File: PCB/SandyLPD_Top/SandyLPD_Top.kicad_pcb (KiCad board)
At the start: 2 copper layers, 30.3 x 23 mm, 18 parts

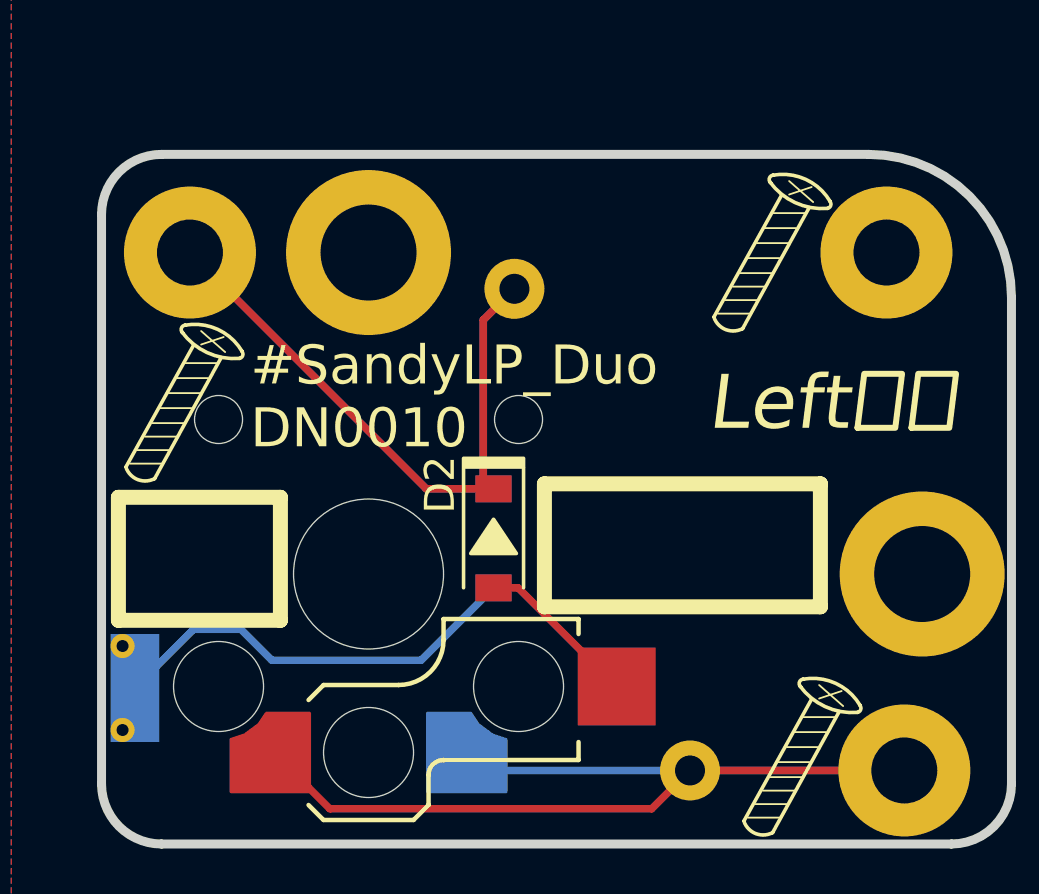
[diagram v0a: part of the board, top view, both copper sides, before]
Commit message: 電源LED位置調整。ボトムA,Bのリセット穴サイズ変更。Fusion用STEP出力。
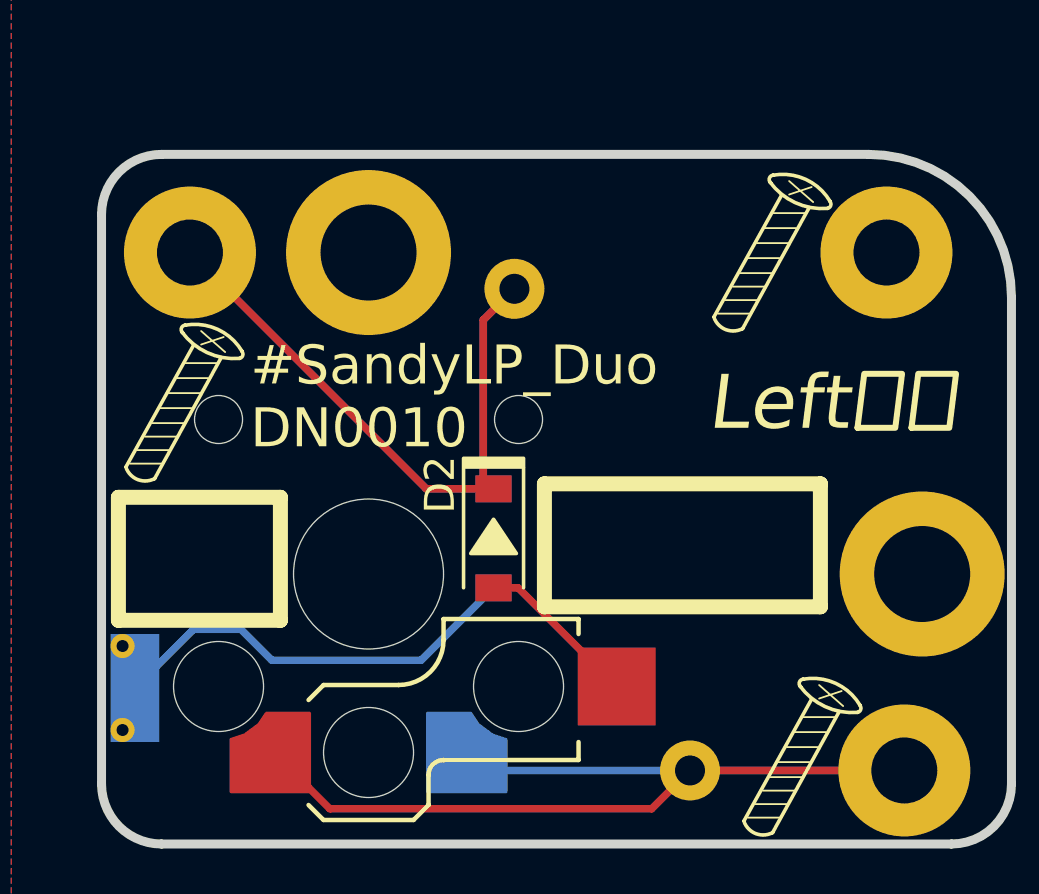
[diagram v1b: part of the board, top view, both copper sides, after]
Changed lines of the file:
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@@
 		(allow_soldermask_bridges_in_footprints no)
 		(aux_axis_origin 19.86781 34.147155)
-		(grid_origin 19.86781 34.147155)
+		(grid_origin 24.63031 36.528405)
 		(pcbplotparams
 			(layerselection 0x00310fc_ffffffff)
@@
 		(fp_arc
 			(start 2.475824 -5.107131)
-			(mid 1.4 -5.3)
+			(mid 1.399999 -5.299999)
 			(end 0.555319 -5.993622)
 			(stroke
@@
 		(at 122.625342 43.973449)
 		(property "Reference" "REF**"
-			(at 0 0.5 360)
+			(at 0 0.5 0)
 			(layer "Cmts.User")
 			(effects
@@
 		)
 		(property "Value" "ICON_Screw_Long_Medium"
-			(at 0 -0.5 360)
+			(at 0 -0.5 0)
 			(layer "F.Fab")
 			(effects
@@
 		)
 		(property "Footprint" "locallib:ICON_Screw_Long_Medium"
-			(at 0 0 360)
+			(at 0 0 0)
 			(layer "F.Fab")
 			(hide yes)
@@
 		)
 		(property "Datasheet" ""
-			(at 0 0 360)
+			(at 0 0 0)
 			(layer "F.Fab")
 			(hide yes)
@@
 		)
 		(property "Description" ""
-			(at 0 0 360)
+			(at 0 0 0)
 			(layer "F.Fab")
 			(hide yes)
@@
 		(fp_arc
 			(start 0.582958 -5.961016)
-			(mid 0.542326 -6.113994)
+			(mid 0.542323 -6.113993)
 			(end 0.665318 -6.21362)
 			(stroke
@@
 		(fp_arc
 			(start 2.475824 -5.107131)
-			(mid 1.399999 -5.299999)
+			(mid 1.4 -5.3)
 			(end 0.555319 -5.993622)
 			(stroke
@@
 		(fp_arc
 			(start 2.475824 -5.107131)
-			(mid 1.4 -5.3)
+			(mid 1.399999 -5.299999)
 			(end 0.555319 -5.993622)
 			(stroke
@@
 		(fp_arc
 			(start 2.475824 5.107132)
-			(mid 2.585568 5.201267)
+			(mid 2.585576 5.201276)
 			(end 2.557784 5.343159)
 			(stroke
@@
 		(fp_arc
 			(start 2.475824 5.107132)
-			(mid 2.585568 5.201267)
+			(mid 2.585576 5.201276)
 			(end 2.557784 5.343159)
 			(stroke
@@
 		(fp_arc
 			(start 0.555319 5.993622)
-			(mid 1.4 5.300002)
+			(mid 1.4 5.300001)
 			(end 2.475824 5.107131)
 			(stroke
@@
 		(tags "test point THT pad")
 		(property "Reference" "T_R0"
-			(at 0 2.070305 360)
+			(at 0 2.070305 0)
 			(layer "B.SilkS")
 			(effects
@@
 		)
 		(property "Value" "Conn_01x01"
-			(at 0 -2.05 360)
+			(at 0 -2.05 0)
 			(layer "B.Fab")
 			(effects
@@
 		)
 		(fp_text user "${REFERENCE}"
-			(at 0 2 360)
+			(at 0 2 0)
 			(layer "B.Fab")
 			(effects
@@
 		(fp_arc
 			(start 2.475824 5.107132)
-			(mid 2.585568 5.201267)
+			(mid 2.585576 5.201276)
 			(end 2.557784 5.343159)
 			(stroke

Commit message: ネジ穴にスルーホールタップのアイコンを追加
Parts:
- added REF**: ICON_Through-hole_Tap, locallib:ICON_Through-hole_Tap, B.Cu at (129.4, 39.8)
- added REF**: ICON_Through-hole_Tap, locallib:ICON_Through-hole_Tap, F.Cu at (129.4, 39.8)
- added REF**: ICON_Through-hole_Tap, locallib:ICON_Through-hole_Tap, F.Cu at (142.7, 45.4)
- added REF**: ICON_Through-hole_Tap, locallib:ICON_Through-hole_Tap, B.Cu at (142.4, 45.9)
- moved REF** 0.54 mm to (143.7, 39.1)
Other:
- board text added: "Left 左 Back Side"
- board text added: "Right 右 Back Side"
- board text removed: "Left 左"
- board text removed: "Right 右"

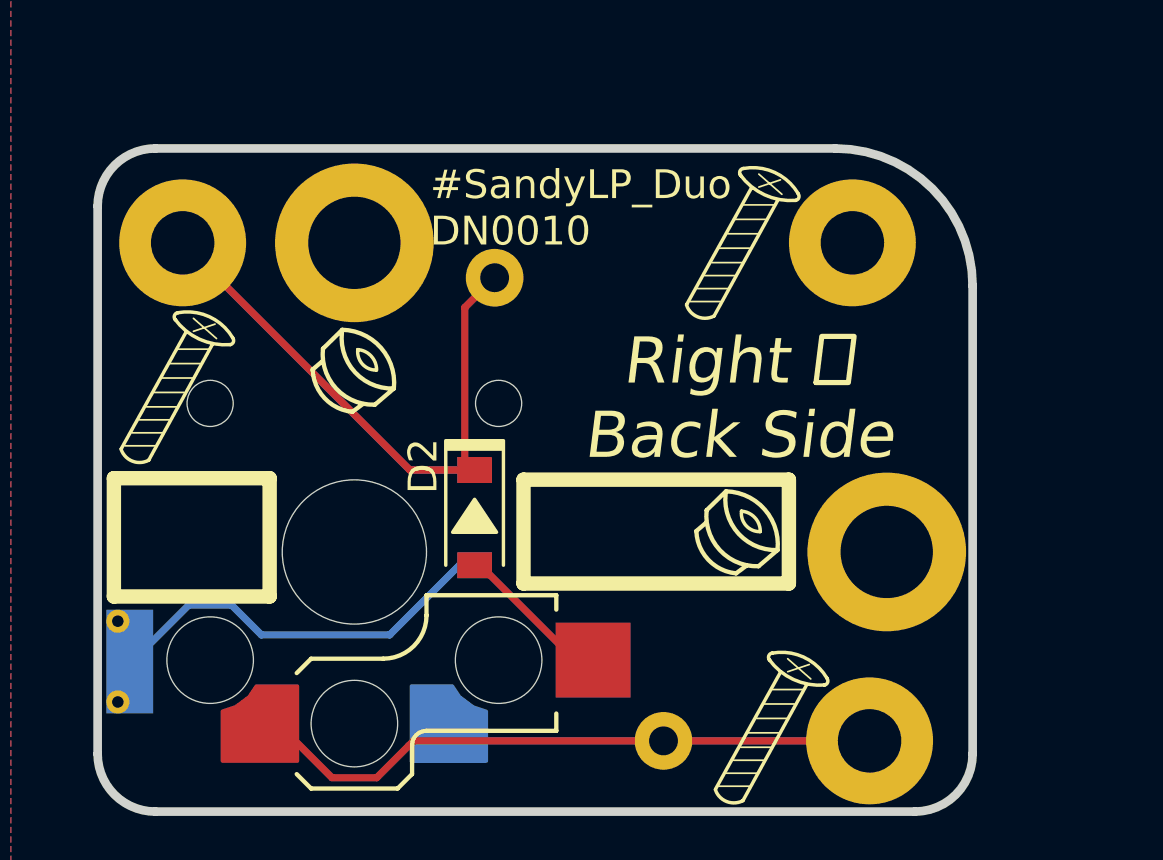
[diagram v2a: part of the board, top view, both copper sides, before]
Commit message: 間違い防止のシルク #30
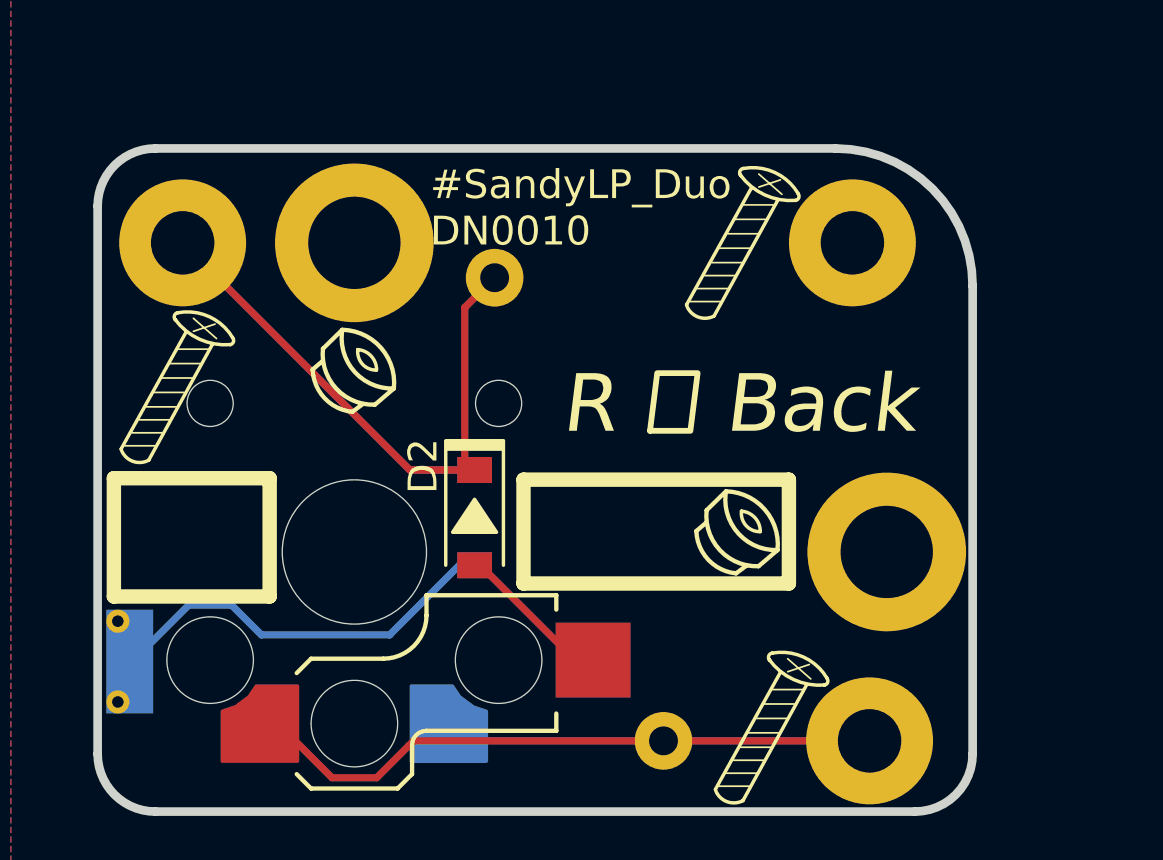
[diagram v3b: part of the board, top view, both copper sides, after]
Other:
- board text added: "L 左 Back"
- board text added: "R 右 Back"
- board text removed: "Left 左 Back Side"
- board text removed: "Right 右 Back Side"
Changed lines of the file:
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@@
 		(fp_arc
 			(start 2.475824 -5.107131)
-			(mid 1.399999 -5.299999)
+			(mid 1.4 -5.3)
 			(end 0.555319 -5.993622)
 			(stroke
@@
 		(fp_arc
 			(start 0.729448 -0.077979)
-			(mid 0.250509 -0.290344)
+			(mid 0.25051 -0.290344)
 			(end 0.092873 -0.789976)
 			(stroke
@@
 		(fp_arc
 			(start 2.475824 -5.107131)
-			(mid 1.4 -5.3)
+			(mid 1.399999 -5.299999)
 			(end 0.555319 -5.993622)
 			(stroke
@@
 		(fp_arc
 			(start 2.475824 -5.107131)
-			(mid 1.399999 -5.299999)
+			(mid 1.4 -5.3)
 			(end 0.555319 -5.993622)
 			(stroke
@@
 		(fp_arc
 			(start 0.729448 -0.077979)
-			(mid 0.250509 -0.290344)
+			(mid 0.25051 -0.290344)
 			(end 0.092873 -0.789976)
 			(stroke
@@
 			(layer "F.SilkS")
 		)
-		(group ""
-			(members "10583bed-aab3-457f-b2ae-f3b5453b8340" "38793d8d-a27c-4080-ae1c-5bc01cf71245"
-				"3ed98f41-62c1-480d-b26d-36dc4ac3c762" "4bf3dc3f-affc-4877-b134-b3363bf5cef2"
-				"53d0ed37-4d95-44d2-b473-0a9a16a8503c" "a00f956a-55b7-46e8-802e-5baff904af2b"
-				"b080e6b3-1454-4fc5-b8b4-c70b5498519d" "d03374e9-98f6-454e-8289-46865e659acf"
-				"f62ba8d0-430f-4730-8b76-93be139405e9" "f8a60fd9-4eb6-4c55-8373-fa38d0a8137c"
-			)
-		)
 	)
 	(footprint "locallib:ICON_Through-hole_Tap"
@@
 			(layer "B.SilkS")
 		)
-		(group ""
-			(members "10583bed-aab3-457f-b2ae-f3b5453b8340" "38793d8d-a27c-4080-ae1c-5bc01cf71245"
-				"3ed98f41-62c1-480d-b26d-36dc4ac3c762" "4bf3dc3f-affc-4877-b134-b3363bf5cef2"
-				"53d0ed37-4d95-44d2-b473-0a9a16a8503c" "a00f956a-55b7-46e8-802e-5baff904af2b"
-				"b080e6b3-1454-4fc5-b8b4-c70b5498519d" "d03374e9-98f6-454e-8289-46865e659acf"
-				"f62ba8d0-430f-4730-8b76-93be139405e9" "f8a60fd9-4eb6-4c55-8373-fa38d0a8137c"
-			)
-		)
 	)
 	(footprint "locallib:Kailh_socket_ChocV2_for_Reverse"
@@
 			(layer "B.SilkS")
 		)
-		(group ""
-			(members "10583bed-aab3-457f-b2ae-f3b5453b8340" "38793d8d-a27c-4080-ae1c-5bc01cf71245"
-				"3ed98f41-62c1-480d-b26d-36dc4ac3c762" "4bf3dc3f-affc-4877-b134-b3363bf5cef2"
-				"53d0ed37-4d95-44d2-b473-0a9a16a8503c" "a00f956a-55b7-46e8-802e-5baff904af2b"
-				"b080e6b3-1454-4fc5-b8b4-c70b5498519d" "d03374e9-98f6-454e-8289-46865e659acf"
-				"f62ba8d0-430f-4730-8b76-93be139405e9" "f8a60fd9-4eb6-4c55-8373-fa38d0a8137c"
-			)
-		)
 	)
 	(gr_rect
@@
 		(layer "F.SilkS")
 	)
-	(gr_text "Left　左\nBack Side"
-		(at 142.93031 40.828405 0)
+	(gr_text "L 左 Back"
+		(at 143.03031 40.928405 0)
 		(layer "B.SilkS" knockout)
 		(effects
 			(font
-				(size 1.6 1.6)
-				(thickness 0.18)
+				(size 2 2)
+				(thickness 0.2)
 				(italic yes)
 			)
@@
 		)
 	)
-	(gr_text "Right 右\nBack Side"
-		(at 142.73031 40.728405 0)
+	(gr_text "R 右 Back"
+		(at 142.73031 40.928405 0)
 		(layer "F.SilkS" knockout)
 		(effects
 			(font
-				(size 1.6 1.6)
-				(thickness 0.18)
+				(size 2 2)
+				(thickness 0.2)
 				(italic yes)
 			)

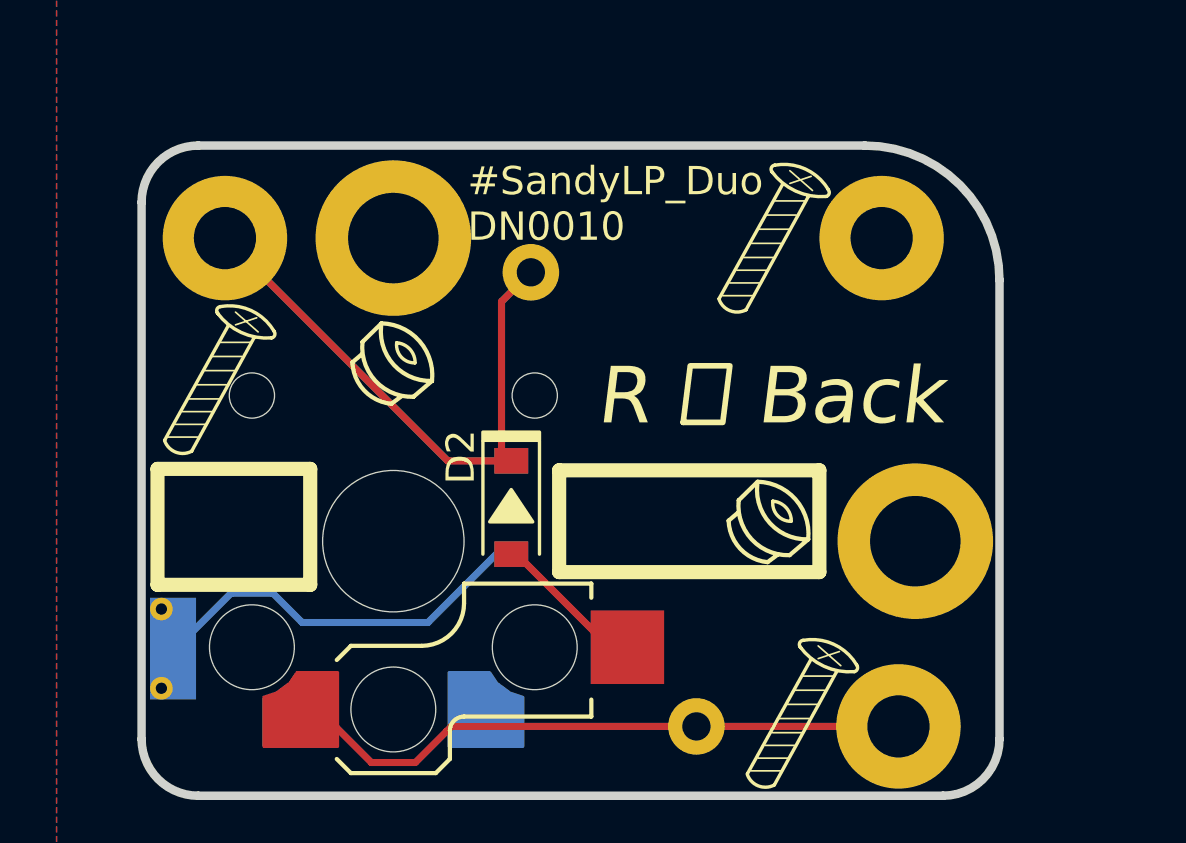
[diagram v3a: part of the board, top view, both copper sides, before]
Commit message: ゴムシート貼り付け指標を調整
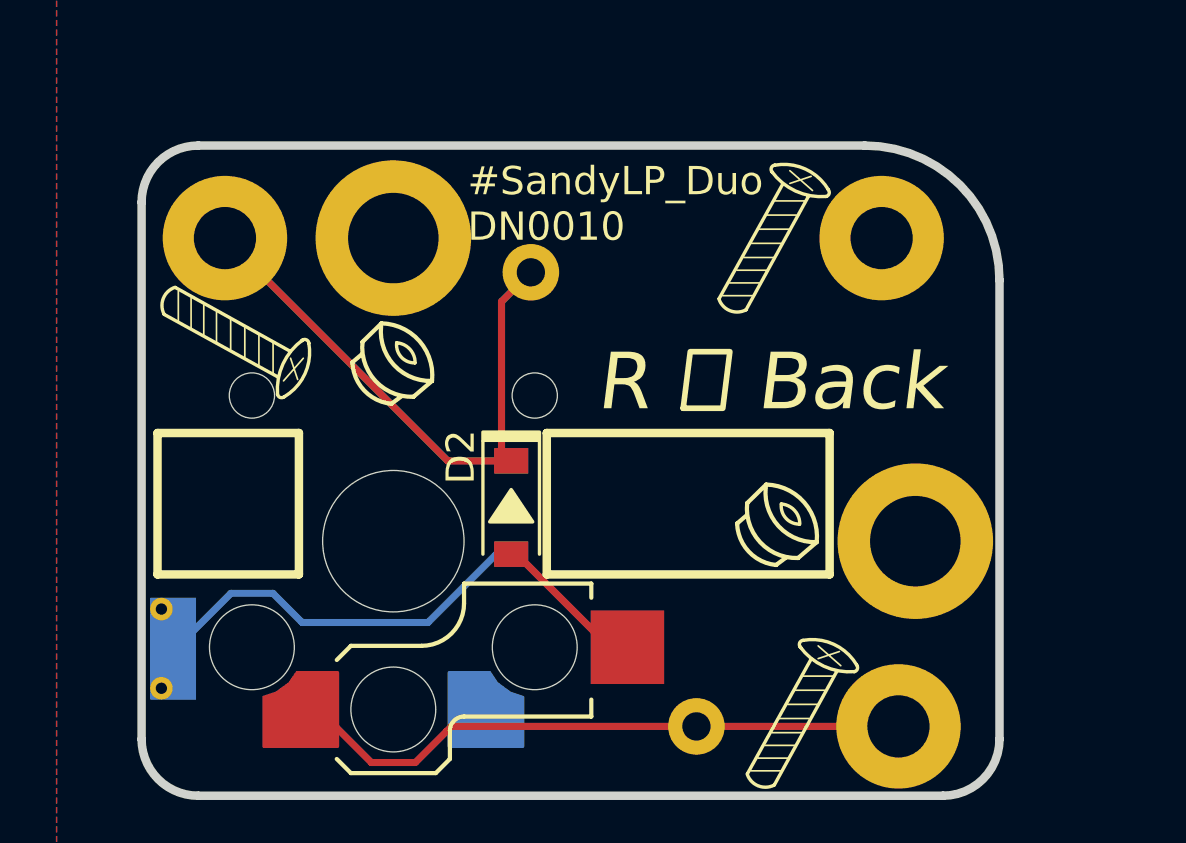
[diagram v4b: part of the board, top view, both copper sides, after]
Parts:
- moved REF** 6.09 mm to (120.2, 38.4), turned to -90 degrees
- moved REF** 0.72 mm to (143.0, 45.5)
- moved REF** 0.32 mm to (143.0, 45.5)
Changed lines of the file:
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@@
 		(fp_arc
 			(start 2.475824 -5.107131)
-			(mid 1.4 -5.3)
+			(mid 1.399999 -5.299999)
 			(end 0.555319 -5.993622)
 			(stroke
@@
 		(fp_arc
 			(start 0.729448 -0.077979)
-			(mid 0.25051 -0.290344)
+			(mid 0.250512 -0.290345)
 			(end 0.092873 -0.789976)
 			(stroke
@@
 		(locked yes)
 		(layer "F.Cu")
-		(at 122.625342 43.973449)
+		(at 120.204016 38.385937 -90)
 		(property "Reference" "REF**"
-			(at 0 0.5 0)
+			(at 0 0.5 90)
 			(layer "Cmts.User")
 			(effects
@@
 		)
 		(property "Value" "ICON_Screw_Long_Medium"
-			(at 0 -0.5 0)
+			(at 0 -0.5 90)
 			(layer "F.Fab")
 			(effects
@@
 		)
 		(property "Footprint" "locallib:ICON_Screw_Long_Medium"
-			(at 0 0 0)
+			(at 0 0 90)
 			(layer "F.Fab")
 			(hide yes)
@@
 		)
 		(property "Datasheet" ""
-			(at 0 0 0)
+			(at 0 0 90)
 			(layer "F.Fab")
 			(hide yes)
@@
 		)
 		(property "Description" ""
-			(at 0 0 0)
+			(at 0 0 90)
 			(layer "F.Fab")
 			(hide yes)
@@
 		)
 		(fp_line
-			(start 0.95 -5.55)
-			(end -1.3 -1.5)
+			(start 1.85 -5.1)
+			(end -0.35 -1.1)
 			(stroke
 				(width 0.12)
@@
 		)
 		(fp_line
-			(start 1.200117 -6.018574)
-			(end 2.000117 -5.318574)
+			(start 0.95 -5.55)
+			(end -1.3 -1.5)
 			(stroke
-				(width 0.06)
+				(width 0.12)
 				(type solid)
 			)
@@
 		)
 		(fp_line
-			(start 1.85 -5.1)
-			(end -0.35 -1.1)
+			(start 1.950117 -5.818574)
+			(end 1.200117 -5.568574)
 			(stroke
-				(width 0.12)
+				(width 0.06)
 				(type solid)
 			)
@@
 		)
 		(fp_line
-			(start 1.950117 -5.818574)
-			(end 1.200117 -5.568574)
+			(start 1.200117 -6.018574)
+			(end 2.000117 -5.318574)
 			(stroke
 				(width 0.06)
@@
 		)
 		(fp_arc
-			(start 0.582958 -5.961016)
-			(mid 0.542323 -6.113993)
-			(end 0.665318 -6.21362)
+			(start 2.475824 -5.107131)
+			(mid 1.4 -5.3)
+			(end 0.555319 -5.993622)
 			(stroke
 				(width 0.12)
-				(type default)
+				(type solid)
 			)
 			(layer "F.SilkS")
 		)
 		(fp_arc
-			(start 0.665318 -6.21362)
-			(mid 1.74926 -6.077071)
-			(end 2.5615 -5.346425)
+			(start 2.557784 -5.343159)
+			(mid 2.58557 -5.201266)
+			(end 2.475824 -5.107132)
 			(stroke
 				(width 0.12)
-				(type solid)
+				(type default)
 			)
 			(layer "F.SilkS")
 		)
 		(fp_arc
-			(start 2.475824 -5.107131)
-			(mid 1.399999 -5.299999)
-			(end 0.555319 -5.993622)
+			(start 0.582958 -5.961016)
+			(mid 0.542323 -6.113993)
+			(end 0.665318 -6.21362)
 			(stroke
 				(width 0.12)
-				(type solid)
+				(type default)
 			)
 			(layer "F.SilkS")
 		)
 		(fp_arc
-			(start 2.557784 -5.343159)
-			(mid 2.58557 -5.201266)
-			(end 2.475824 -5.107132)
+			(start 0.665318 -6.21362)
+			(mid 1.74926 -6.077071)
+			(end 2.5615 -5.346425)
 			(stroke
 				(width 0.12)
-				(type default)
+				(type solid)
 			)
 			(layer "F.SilkS")
@@
 		(fp_arc
 			(start 2.475824 -5.107131)
-			(mid 1.4 -5.3)
+			(mid 1.399999 -5.299999)
 			(end 0.555319 -5.993622)
 			(stroke
@@
 		(locked yes)
 		(layer "F.Cu")
-		(at 142.73031 45.428405)
+		(at 143.030309 45.528403)
 		(property "Reference" "REF**"
 			(at 0 -0.5 0)
@@
 		(fp_arc
 			(start 0.729448 -0.077979)
-			(mid 0.25051 -0.290344)
+			(mid 0.250512 -0.290345)
 			(end 0.092873 -0.789976)
 			(stroke
@@
 		(locked yes)
 		(layer "B.Cu")
-		(at 142.43031 45.928405 180)
+		(at 143.03031 45.528405 180)
 		(property "Reference" "REF**"
 			(at 0 0.5 0)
@@
 	)
 	(gr_rect
-		(start 135.26781 43.847155)
-		(end 144.46781 47.947155)
+		(start 134.83031 42.228405)
+		(end 144.83031 47.228405)
 		(stroke
-			(width 0.5)
+			(width 0.3)
 			(type solid)
 		)
@@
 	)
 	(gr_rect
-		(start 121.06781 43.047155)
-		(end 126.46781 47.147155)
+		(start 121.06781 42.228405)
+		(end 126.06781 47.228405)
 		(stroke
-			(width 0.5)
+			(width 0.3)
 			(type solid)
 		)
@@
 	)
 	(gr_rect
-		(start 135.26781 43.547155)
-		(end 144.46781 47.147155)
+		(start 134.83031 42.228405)
+		(end 144.83031 47.228405)
 		(stroke
-			(width 0.5)
+			(width 0.3)
 			(type solid)
 		)
@@
 	)
 	(gr_rect
-		(start 121.06781 43.497155)
-		(end 126.46781 47.597155)
+		(start 121.06781 42.228405)
+		(end 126.06781 47.228405)
 		(stroke
-			(width 0.5)
+			(width 0.3)
 			(type solid)
 		)
@@
 	)
 	(gr_text "L 左 Back"
-		(at 143.03031 40.928405 0)
+		(at 143.03031 40.428405 0)
 		(layer "B.SilkS" knockout)
 		(effects
@@
 	)
 	(gr_text "R 右 Back"
-		(at 142.73031 40.928405 0)
+		(at 142.73031 40.428405 0)
 		(layer "F.SilkS" knockout)
 		(effects
